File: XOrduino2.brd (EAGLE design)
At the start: 81.3 x 59.8 mm, 82 parts, among them J1 2.5mm, J2 2.5mm, J3 2.5mm, J4 2.5mm, J5 Batt In, J6 MOT R, J7 MOT L, P1 10k, Q1 ALS-PT204-6C/L177, SW1 RESET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

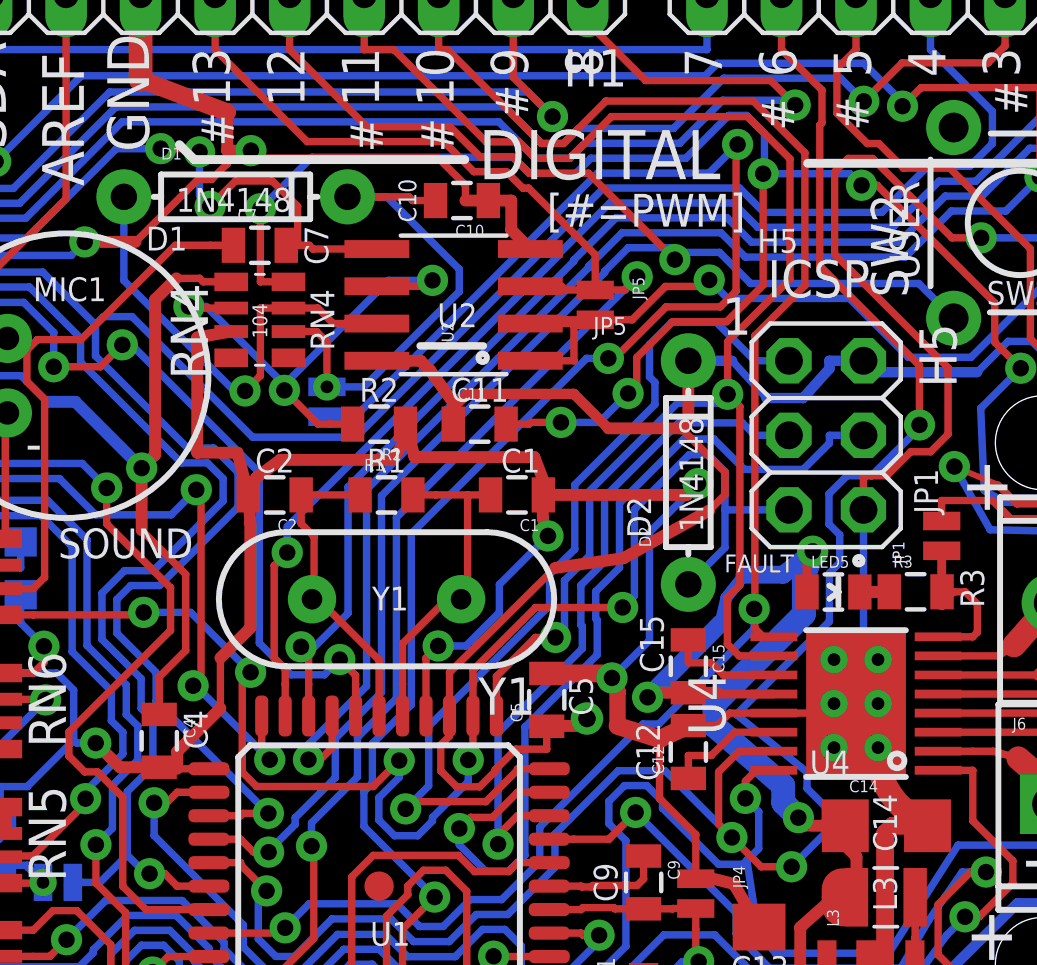
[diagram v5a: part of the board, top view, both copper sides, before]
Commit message: XOrduino2 v8.  Rename nets for better manual auditing, silkscreen tweaks.
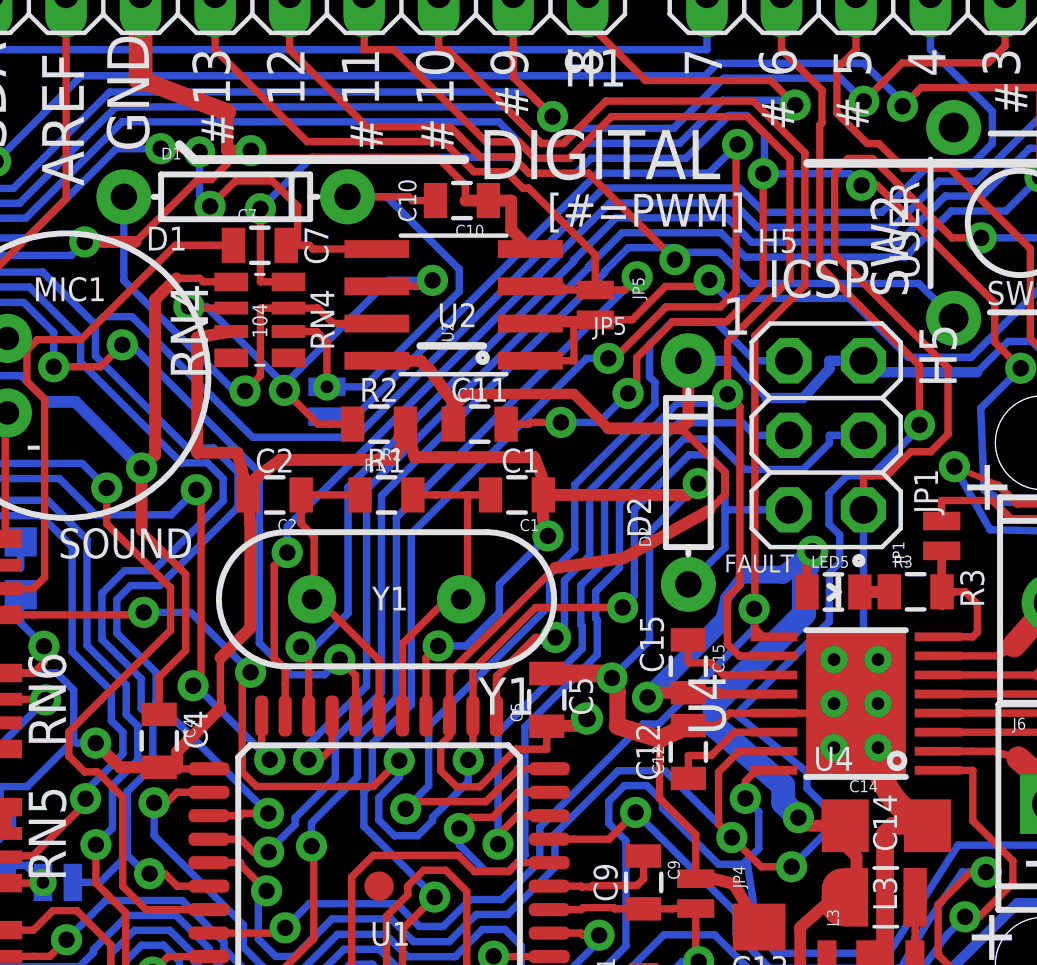
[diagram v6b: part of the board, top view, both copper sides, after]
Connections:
- net N$1 renamed LED3_ANODE
- net N$10 renamed U4_VINT
- net N$11 renamed OPAMP1_P
- net N$12 renamed U4_NFAULT
- net N$13 renamed U6_ANODE
- net N$14 renamed U3_CONT
- net N$15 renamed U5_ANODE
- net N$16 renamed OPAMP1_OUT
- net N$18 renamed LED5_CATHODE
- net N$19 renamed U4_BISEN
- net N$2 renamed LED1_ANODE
- net N$20 renamed U4_AISEN
- net N$21 renamed U5_COLLECTOR
- net N$22 renamed U6_COLLECTOR
- net N$3 renamed LED4_ANODE
- net N$4 renamed LED2_ANODE
- net N$5 renamed OPAMP1_M
- net N$6 renamed IO13_MIRROR
- net N$7 renamed U4_VCP
- net N$8 renamed U4_NSLEEP
- net N$9 renamed MIC_IN
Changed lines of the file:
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@@
 <layer number="16" name="Bottom" color="1" fill="1" visible="no" active="yes"/>
 <layer number="17" name="Pads" color="2" fill="1" visible="yes" active="yes"/>
-<layer number="18" name="Vias" color="14" fill="1" visible="yes" active="yes"/>
+<layer number="18" name="Vias" color="14" fill="1" visible="no" active="yes"/>
 <layer number="19" name="Unrouted" color="6" fill="1" visible="yes" active="yes"/>
 <layer number="20" name="Dimension" color="15" fill="2" visible="yes" active="yes"/>
 <layer number="21" name="tPlace" color="7" fill="1" visible="yes" active="yes"/>
 <layer number="22" name="bPlace" color="7" fill="1" visible="no" active="yes"/>
-<layer number="23" name="tOrigins" color="15" fill="1" visible="no" active="yes"/>
+<layer number="23" name="tOrigins" color="15" fill="1" visible="yes" active="yes"/>
 <layer number="24" name="bOrigins" color="15" fill="1" visible="no" active="yes"/>
 <layer number="25" name="tNames" color="5" fill="1" visible="no" active="yes"/>
@@
 <layer number="27" name="tValues" color="7" fill="1" visible="no" active="yes"/>
 <layer number="28" name="bValues" color="7" fill="1" visible="no" active="yes"/>
-<layer number="29" name="tStop" color="2" fill="3" visible="no" active="yes"/>
+<layer number="29" name="tStop" color="2" fill="3" visible="yes" active="yes"/>
 <layer number="30" name="bStop" color="5" fill="6" visible="no" active="yes"/>
 <layer number="31" name="tCream" color="7" fill="4" visible="no" active="yes"/>
@@
 <text x="71.755" y="27.305" size="0.8128" layer="21" ratio="22" align="bottom-center">J7</text>
 <text x="76.835" y="31.115" size="0.8128" layer="21" ratio="22" rot="R90" align="bottom-center">RN7</text>
-<text x="62.611" y="24.257" size="0.8128" layer="21" ratio="22" align="bottom-center">U4</text>
+<text x="62.738" y="24.384" size="0.8128" layer="21" ratio="22" align="bottom-center">U4</text>
 <text x="76.2" y="10.16" size="0.8128" layer="21" ratio="22" rot="R90" align="bottom-center">SW4</text>
 <text x="76.835" y="21.59" size="0.8128" layer="21" ratio="22" rot="R180" align="bottom-center">Q1</text>
@@
 </element>
 <element name="H1" library="SmartPrj" package="1X10" value="10x1F-H8.5" x="42.926" y="50.8" rot="R180"/>
-<element name="D2" library="SparkFun-DiscreteSemi" package="DIODE-1N4148" value="1N4148" x="57.785" y="34.544" rot="R90"/>
+<element name="D2" library="SparkFun-DiscreteSemi" package="DIODE-1N4148" value="1N4148" x="57.785" y="34.544" smashed="yes" rot="R90">
+<attribute name="NAME" x="56.515" y="32.004" size="0.4064" layer="25" rot="R90"/>
+<attribute name="VALUE" x="58.293" y="32.512" size="0.8128" layer="51" rot="R90"/>
+</element>
 <element name="SW1" library="SparkFun-Electromechanical" package="TACTILE-PTH" value="RESET" x="26.67" y="22.225" rot="R270"/>
 <element name="X1" library="SparkFun-Connectors" package="USB-A-PCB" value="USBPCB" x="5.08" y="21.971"/>
@@
 <element name="C7" library="SparkFun-Passives" package="0805" value="100n" x="43.18" y="42.291"/>
 <element name="R2" library="SparkFun-Passives" package="0805" value="2.2k" x="47.244" y="36.195" rot="R180"/>
-<element name="D1" library="SparkFun-DiscreteSemi" package="DIODE-1N4148" value="1N4148" x="42.355" y="43.942"/>
+<element name="D1" library="SparkFun-DiscreteSemi" package="DIODE-1N4148" value="1N4148" x="42.355" y="43.942" smashed="yes">
+<attribute name="NAME" x="39.815" y="45.212" size="0.4064" layer="25"/>
+<attribute name="VALUE" x="40.323" y="43.434" size="0.8128" layer="51"/>
+</element>
 <element name="C10" library="SparkFun-Passives" package="0805" value="0.22uF" x="50.068" y="43.815" rot="R180"/>
 <element name="C11" library="SparkFun-Passives" package="0805" value="0.33uF" x="50.673" y="36.195"/>
@@
 <wire x1="59.6278" y1="36.2393" x2="60.0531" y2="35.814" width="0.254" layer="16"/>
 </signal>
-<signal name="N$3">
+<signal name="LED4_ANODE">
 <contactref element="LED4" pad="A"/>
 <contactref element="RN3" pad="2"/>
@@
 <contactref element="H3" pad="4"/>
 </signal>
-<signal name="N$2">
+<signal name="LED1_ANODE">
 <contactref element="LED1" pad="A"/>
 <contactref element="RN3" pad="1"/>
@@
 <wire x1="67.6254" y1="14.3429" x2="64.3544" y2="8.3182" width="0.254" layer="16"/>
 </signal>
-<signal name="N$9">
+<signal name="MIC_IN">
 <contactref element="MIC1" pad="1"/>
 <contactref element="C7" pad="1"/>
@@
 <wire x1="40.2988" y1="42.291" x2="41.4989" y2="42.291" width="0.254" layer="1"/>
 </signal>
-<signal name="N$11">
+<signal name="OPAMP1_P">
 <contactref element="C7" pad="2"/>
 <contactref element="U2" pad="5"/>
@@
 <wire x1="41.0158" y1="45.5843" x2="39.8012" y2="45.5843" width="0.254" layer="1"/>
 </signal>
-<signal name="N$5">
+<signal name="OPAMP1_M">
 <contactref element="U2" pad="6"/>
 <contactref element="R2" pad="2"/>
@@
 <wire x1="48.8629" y1="40.894" x2="49.0639" y2="41.095" width="0.254" layer="1"/>
 </signal>
-<signal name="N$16">
+<signal name="OPAMP1_OUT">
 <contactref element="U2" pad="7"/>
 <contactref element="D1" pad="A"/>
@@
 <wire x1="26.67" y1="40.64" x2="26.67" y2="38.989" width="0.4064" layer="16"/>
 </signal>
-<signal name="N$6">
+<signal name="IO13_MIRROR">
 <contactref element="U2" pad="1"/>
 <contactref element="U2" pad="2"/>
@@
 <wire x1="52.4002" y1="38.354" x2="53.8862" y2="38.354" width="0.254" layer="1"/>
 </signal>
-<signal name="N$7">
+<signal name="U4_VCP">
 <contactref element="C15" pad="1"/>
 <contactref element="U4" pad="11"/>
@@
 <wire x1="57.785" y1="28.84" x2="57.785" y2="28.0589" width="0.254" layer="1"/>
 </signal>
-<signal name="N$10">
+<signal name="U4_VINT">
 <contactref element="U4" pad="14"/>
 <contactref element="C12" pad="1"/>
@@
 <wire x1="57.785" y1="24.119" x2="57.785" y2="24.9001" width="0.254" layer="1"/>
 </signal>
-<signal name="N$8">
+<signal name="U4_NSLEEP">
 <contactref element="U4" pad="1"/>
 <contactref element="RN5" pad="7"/>
@@
 <wire x1="34.503" y1="23.139" x2="34.503" y2="22.244" width="0.4064" layer="1"/>
 </signal>
-<signal name="N$12">
+<signal name="U4_NFAULT">
 <contactref element="U4" pad="8"/>
 <contactref element="R3" pad="2"/>
@@
 <wire x1="22.0763" y1="25.0969" x2="22.1739" y2="24.9993" width="0.254" layer="1"/>
 </signal>
-<signal name="N$15">
+<signal name="U5_ANODE">
 <contactref element="U5" pad="1"/>
 <contactref element="RN6" pad="8"/>
@@
 <wire x1="35.0266" y1="30.3784" x2="35.0284" y2="30.3784" width="0.2032" layer="16"/>
 </signal>
-<signal name="N$13">
+<signal name="U6_ANODE">
 <contactref element="U6" pad="1"/>
 <contactref element="RN6" pad="7"/>
@@
 <wire x1="30.4292" y1="22.9616" x2="30.4274" y2="22.9616" width="0.2032" layer="16"/>
 </signal>
-<signal name="N$14">
+<signal name="U3_CONT">
 <contactref element="U3" pad="1"/>
 <contactref element="L3" pad="2"/>
@@
 <wire x1="65.516" y1="20.066" x2="65.516" y2="18.6849" width="0.254" layer="1"/>
 </signal>
-<signal name="N$19">
+<signal name="U4_BISEN">
 <contactref element="U4" pad="6"/>
 <contactref element="RN7" pad="1"/>
@@
 <wire x1="68.356" y1="28.295" x2="66.3" y2="28.295" width="0.254" layer="1"/>
 </signal>
-<signal name="N$20">
+<signal name="U4_AISEN">
 <contactref element="RN7" pad="3"/>
 <contactref element="U4" pad="3"/>
@@
 <wire x1="77.59" y1="29.565" x2="77.59" y2="30.44" width="0.4064" layer="1"/>
 </signal>
-<signal name="N$1">
+<signal name="LED3_ANODE">
 <contactref element="LED3" pad="A"/>
 <contactref element="RN3" pad="4"/>
@@
 <wire x1="68.961" y1="13.324" x2="67.9799" y2="13.324" width="0.254" layer="1"/>
 </signal>
-<signal name="N$4">
+<signal name="LED2_ANODE">
 <contactref element="LED2" pad="A"/>
 <contactref element="RN3" pad="3"/>
@@
 <wire x1="67.446" y1="11.85" x2="68.4021" y2="11.85" width="0.254" layer="1"/>
 </signal>
-<signal name="N$18">
+<signal name="LED5_CATHODE">
 <contactref element="LED5" pad="C"/>
 <contactref element="R3" pad="1"/>
@@
 <wire x1="63.631" y1="30.473" x2="64.4121" y2="30.473" width="0.4064" layer="1"/>
 </signal>
-<signal name="N$21">
+<signal name="U5_COLLECTOR">
 <contactref element="RN5" pad="6"/>
 <contactref element="U5" pad="3"/>
@@
 <wire x1="31.1404" y1="32.1818" x2="31.1404" y2="32.1801" width="0.2032" layer="16"/>
 </signal>
-<signal name="N$22">
+<signal name="U6_COLLECTOR">
 <contactref element="RN5" pad="5"/>
 <contactref element="U6" pad="3"/>
